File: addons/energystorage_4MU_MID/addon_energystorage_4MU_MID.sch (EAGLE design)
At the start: 31 parts, among them IC1 74HC595D, IC2 74HC595D, Q1 BCP52

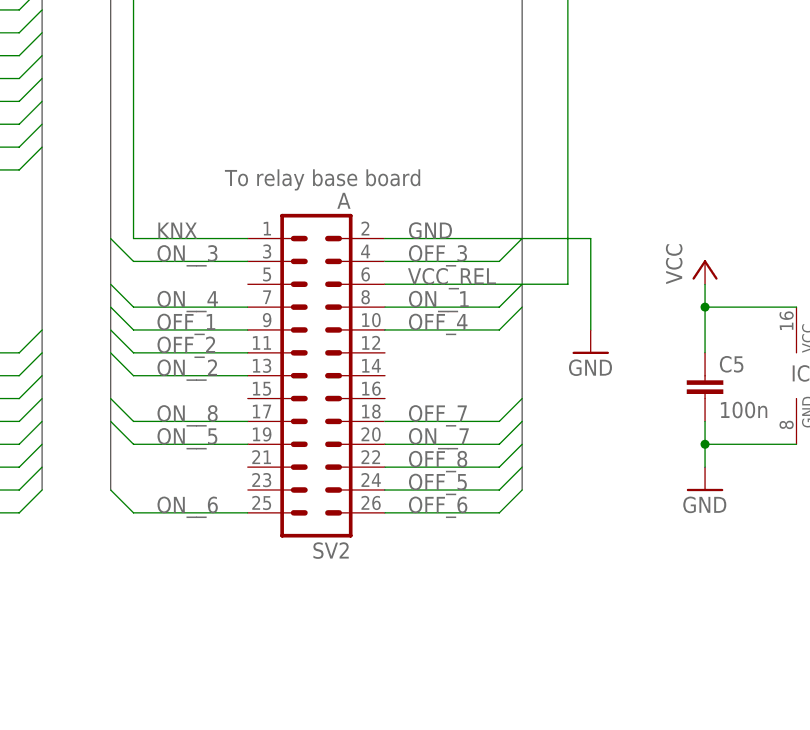
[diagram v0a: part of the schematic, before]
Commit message: [Application - out8 16A - bistable relay - 4TE - BOT] erc edited
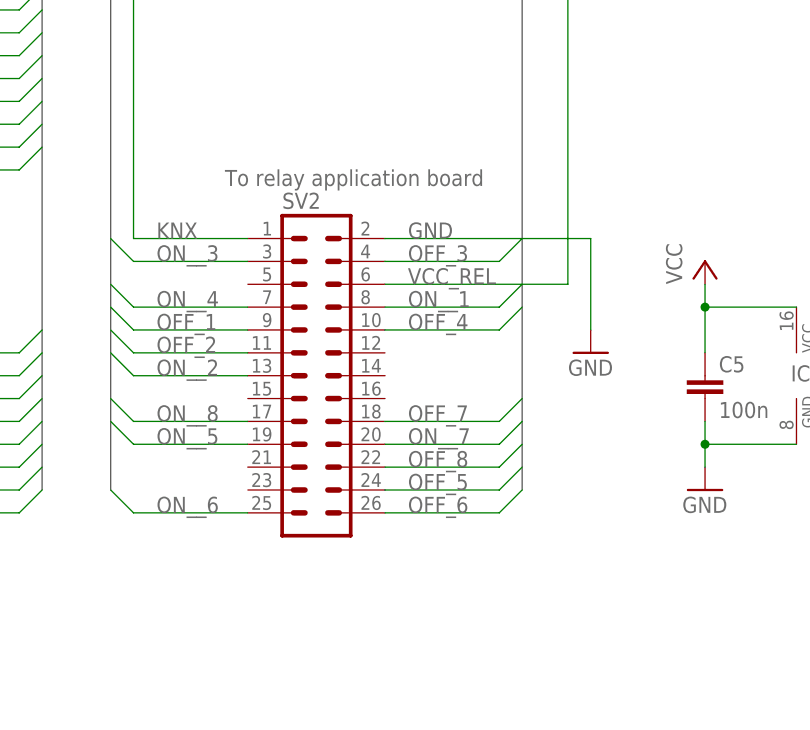
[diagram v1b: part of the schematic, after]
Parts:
- SV1: value (none) -> B
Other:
- note added: "To relay application board"
- note removed: "To relay base board"
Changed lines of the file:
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@@
 <part name="SV2" library="con-harting-ml" deviceset="ML26" device="" value="A"/>
 <part name="GND13" library="supply1" deviceset="GND" device=""/>
-<part name="SV1" library="pinhead" deviceset="PINHD-2X13" device="SMD"/>
+<part name="SV1" library="pinhead" deviceset="PINHD-2X13" device="SMD" value="B"/>
 <part name="P+9" library="supply1" deviceset="VCC" device=""/>
 <part name="GND11" library="supply1" deviceset="GND" device=""/>
@@
 <text x="78.74" y="114.3" size="1.778" layer="104" rot="MR0">PIO0.2 IO5</text>
 <text x="73.66" y="137.16" size="1.778" layer="95" align="top-left">To ARM top controller board</text>
-<text x="271.78" y="119.38" size="1.778" layer="95" align="top-left">To relay base board</text>
+<text x="271.78" y="119.38" size="1.778" layer="95" align="top-left">To relay application board</text>
 <text x="375.412" y="6.096" size="3.81" layer="97">V1.1</text>
 <text x="353.314" y="29.972" size="5.08" layer="97">selfbus.org</text>
@@
 <instance part="GND12" gate="1" x="215.9" y="20.32"/>
 <instance part="LED1" gate="G$1" x="195.58" y="25.4" rot="R90"/>
-<instance part="SV2" gate="1" x="281.94" y="96.52" rot="R180"/>
+<instance part="SV2" gate="1" x="281.94" y="96.52" smashed="yes" rot="R180">
+<attribute name="NAME" x="278.13" y="115.062" size="1.778" layer="95"/>
+</instance>
 <instance part="GND13" gate="1" x="312.42" y="99.06"/>
-<instance part="SV1" gate="A" x="86.36" y="114.3"/>
+<instance part="SV1" gate="A" x="86.36" y="114.3" smashed="yes">
+<attribute name="NAME" x="80.01" y="132.715" size="1.778" layer="95"/>
+</instance>
 <instance part="P+9" gate="VCC" x="60.96" y="134.62"/>
 <instance part="GND11" gate="1" x="73.66" y="99.06"/>
@@
 </instances>
 <busses>
-<bus name="B$2">
+<bus name="ON__[1..8],OFF_[1..8]">
 <segment>
 <wire x1="251.46" y1="83.82" x2="251.46" y2="142.24" width="0.762" layer="92"/>
@@
 </segment>
 </bus>
-<bus name="B$1">
+<bus name="/SSEL,ADC_URAIL,KNX_DC,MISO,MOSI,PROG,RELPWM,SCK">
 <segment>
 <wire x1="160.02" y1="45.72" x2="160.02" y2="236.22" width="0.762" layer="92"/>
